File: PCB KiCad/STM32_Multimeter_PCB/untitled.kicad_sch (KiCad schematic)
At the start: 73 parts, among them J6 Barrel_Jack, J7 Conn_01x02_Pin, J8 Barrel_Jack, J9 Barrel_Jack, K1 G6K-2, Q1 CSD19534Q5A, Q10 BC327, Q11 BC327, Q12 BC327, Q13 BC327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

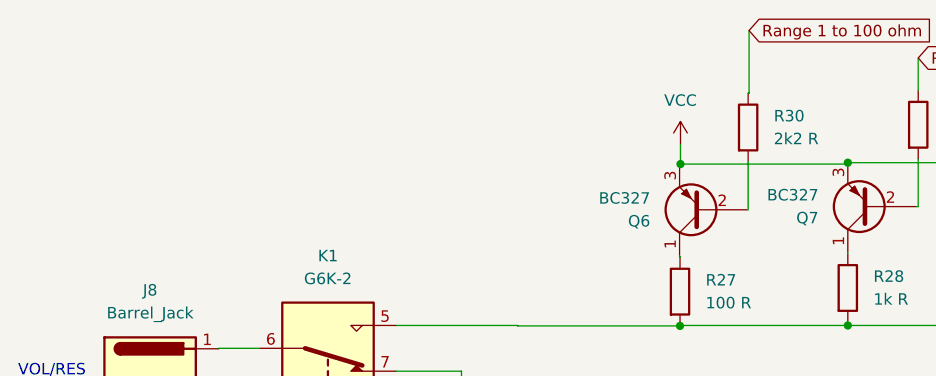
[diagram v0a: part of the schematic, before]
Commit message: Connected measuring circuitry to STM32
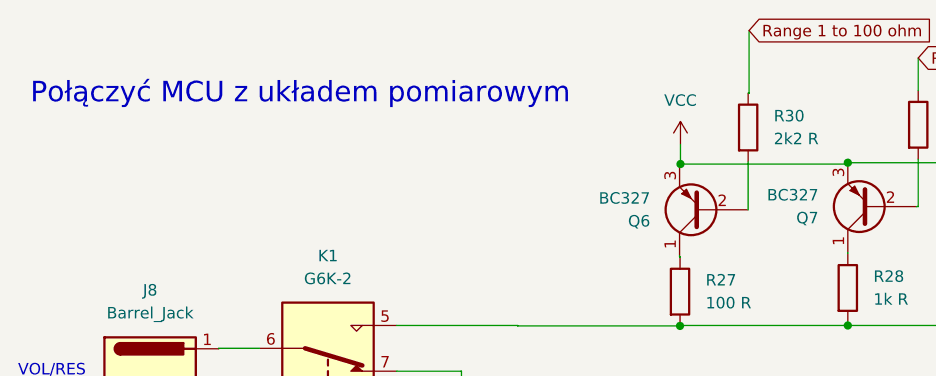
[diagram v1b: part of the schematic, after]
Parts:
- L5: footprint Inductor_SMD:L_Chilisin_BMRB00060650 -> Inductor_SMD:L_Taiyo-Yuden_NR-50xx
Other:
- note added: "Połączyć MCU z układem pomiarowym"
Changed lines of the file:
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@@
     (effects (font (size 1.27 1.27)) (justify left bottom))
+  )
+  (text "Połączyć MCU z układem pomiarowym" (at 14.7828 22.9108 0)
+    (effects (font (size 2.27 2.27)) (justify left bottom))
   )
   (text "COM" (at 186.944 34.4932 0)
@@
       (effects (font (size 1.27 1.27)) (justify left))
     )
-    (property "Footprint" "Inductor_SMD:L_Chilisin_BMRB00060650" (at 221.0308 138.7856 0)
-      (effects (font (size 1.27 1.27)) hide)
-    )
+    (property "Footprint" "Inductor_SMD:L_Taiyo-Yuden_NR-50xx" (at 221.0308 138.7856 0)
+      (effects (font (size 1.27 1.27)) hide)
+    )

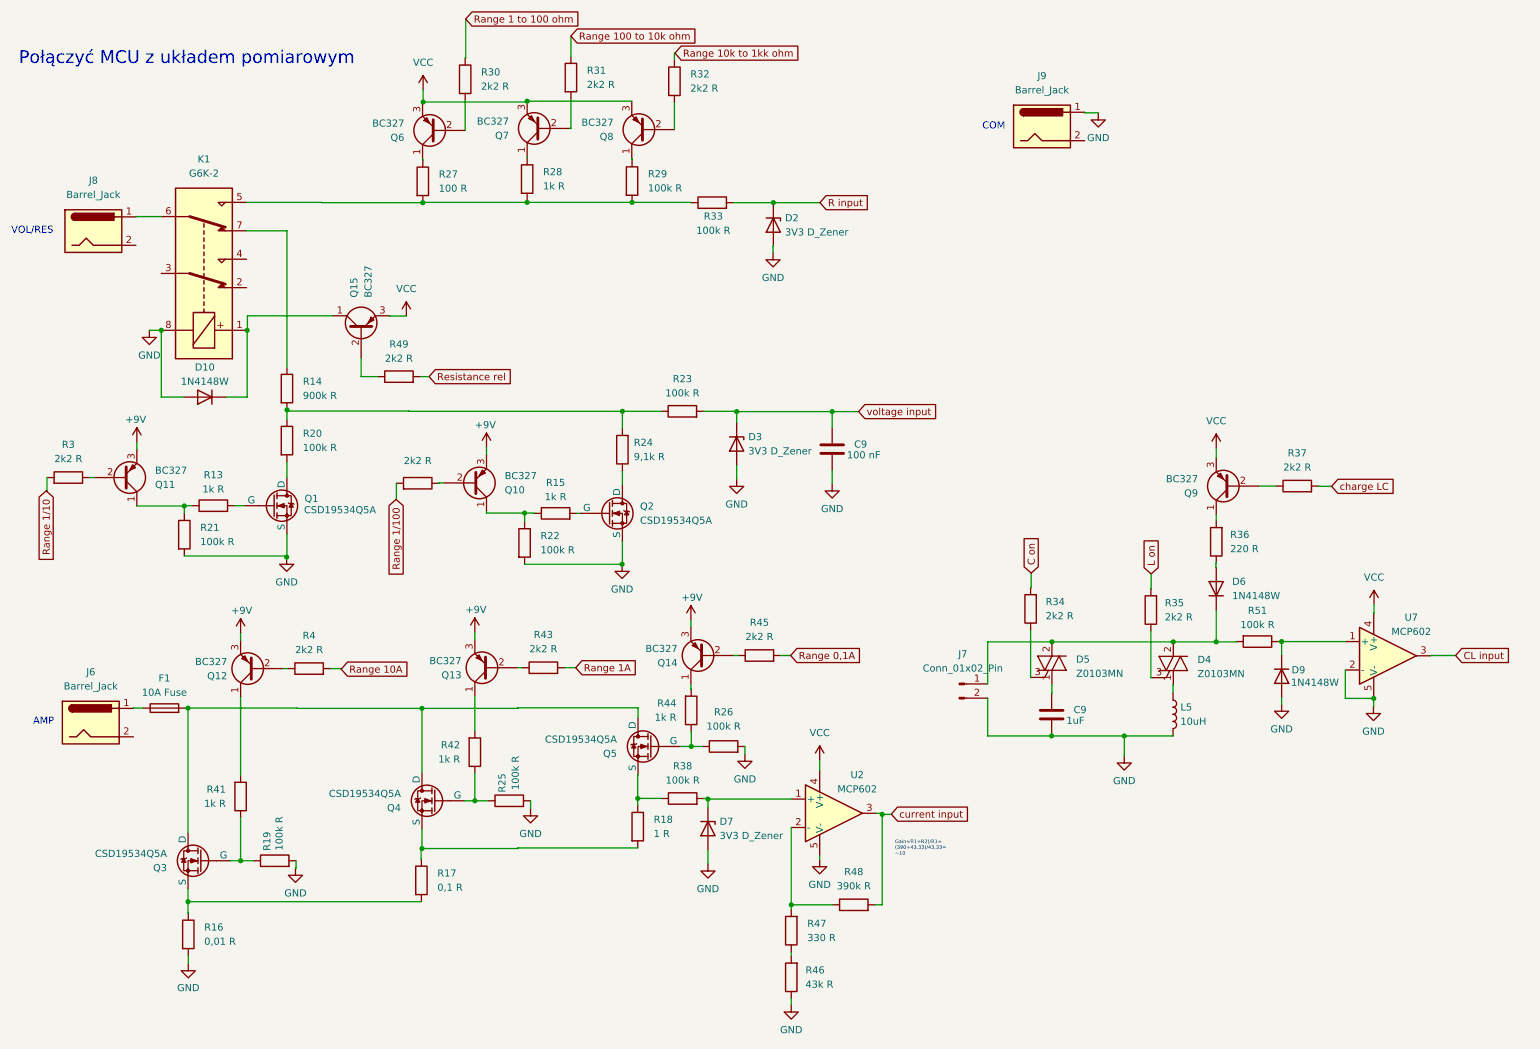
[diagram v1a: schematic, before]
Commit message: Created pcb schematic
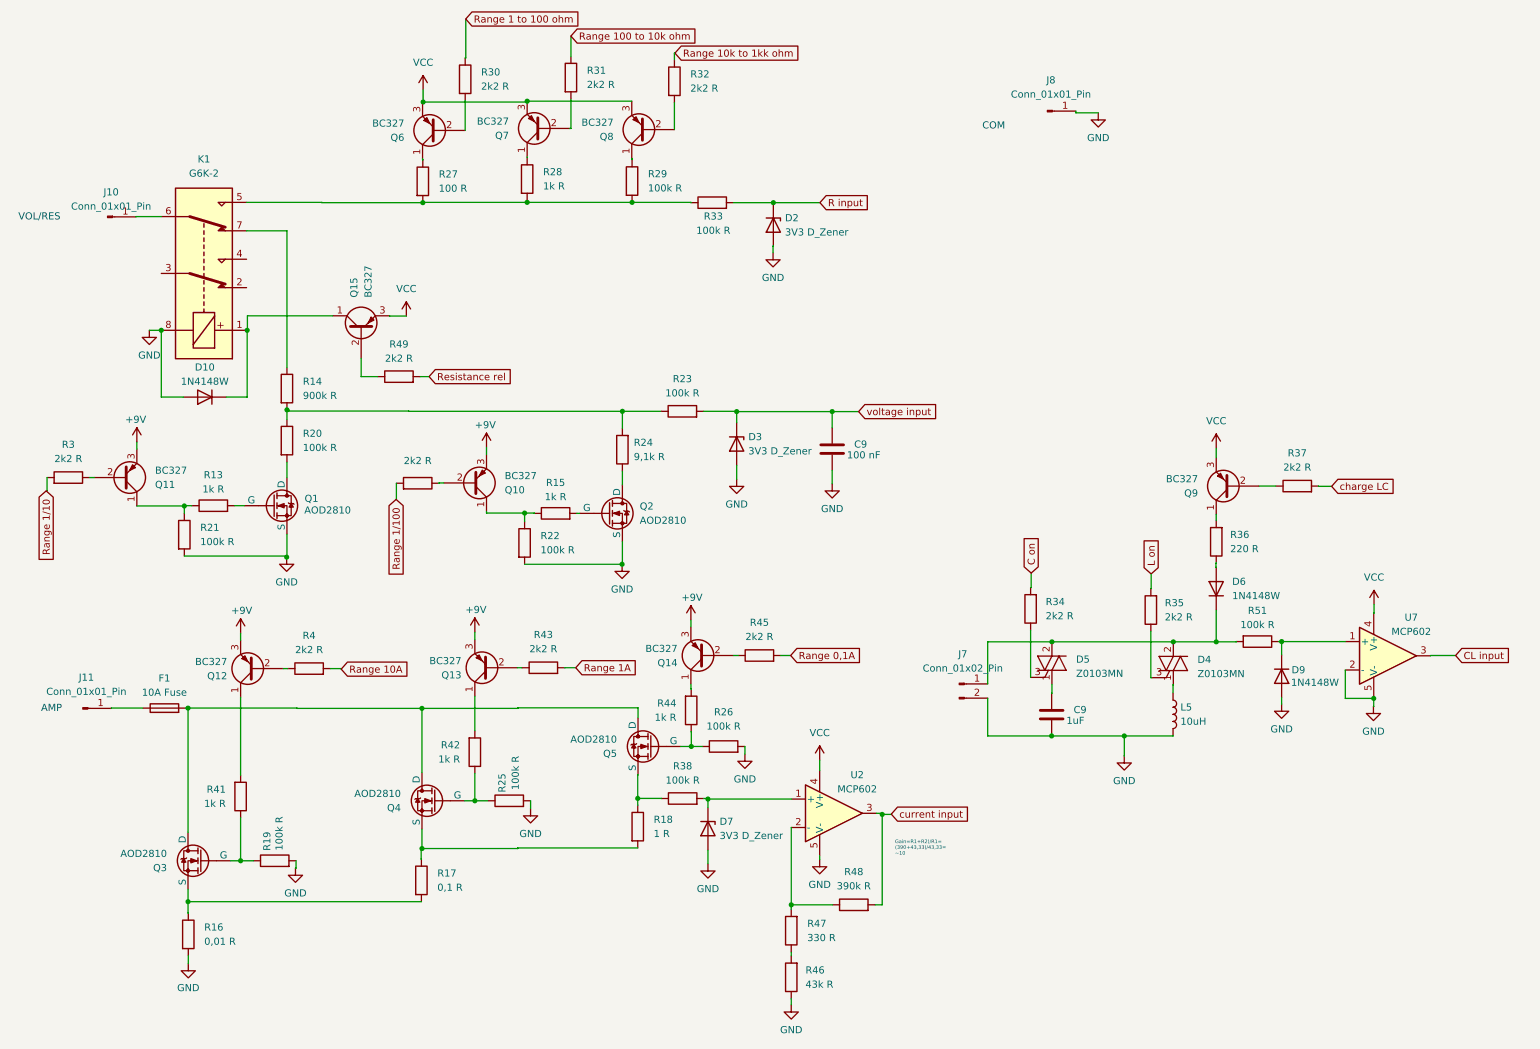
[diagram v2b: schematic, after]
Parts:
- removed J6, J8, J9: Barrel_Jack, Connector_PinHeader_2.54mm:PinHeader_1x01_P2.54mm_Vertical, symbol Connector:Barrel_Jack
- added J10, J11, J8: Conn_01x01_Pin, Connector_PinHeader_2.54mm:PinHeader_1x01_P2.54mm_Vertical, symbol Connector:Conn_01x01_Pin
- Q1, Q2, Q3, Q4, Q5: value CSD19534Q5A -> AOD2810; footprint Package_DFN_QFN:PQFN-8-EP_6x5mm_P1.27mm_Generic -> moje_elementy:TO-252-1
- R16, R17: footprint Resistor_SMD:R_MELF_MMB-0207 -> Resistor_THT:R_Box_L14.0mm_W5.0mm_P9.00mm
- R18: footprint Resistor_SMD:R_MELF_MMB-0207 -> Resistor_THT:R_Axial_DIN0918_L18.0mm_D9.0mm_P25.40mm_Horizontal
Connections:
- net GND: now also J8.1 (Pin_1)
- net at K1.6: now also J10.1 (Pin_1)
- net at F1.1: now also J11.1 (Pin_1)
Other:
- note removed: "Połączyć MCU z układem pomiarowym"

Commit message: routed out signals and power planes
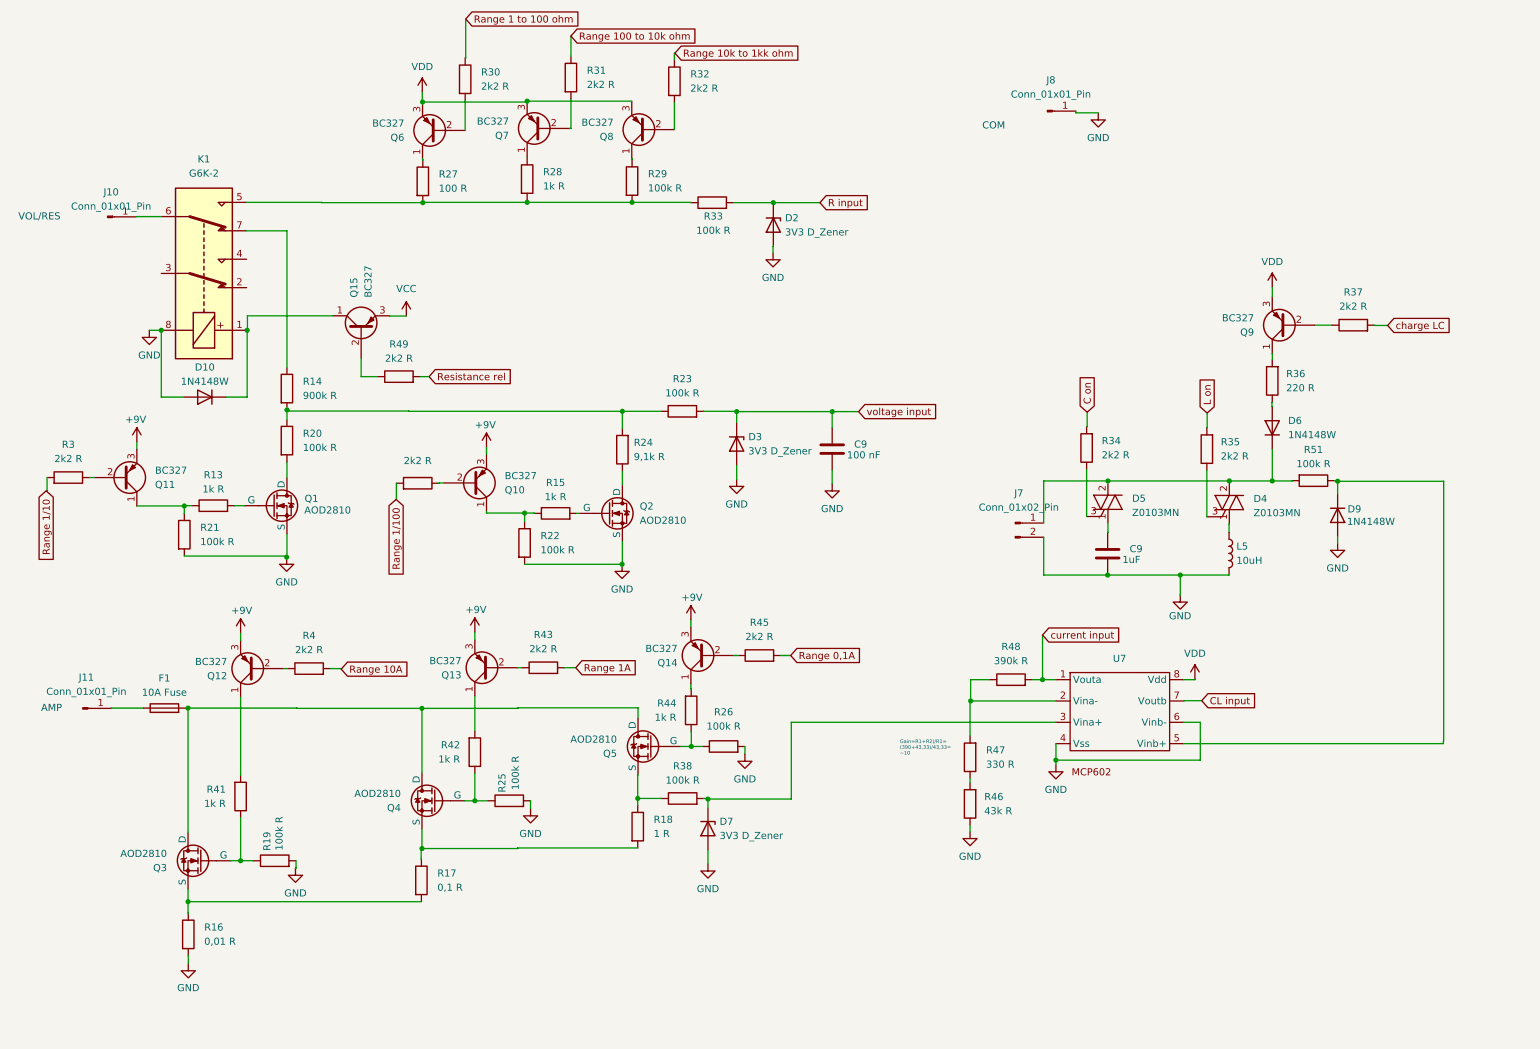
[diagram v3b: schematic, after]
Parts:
- removed U2, U7: MCP602, symbol Simulation_SPICE:OPAMP
- added U7: ~, Package_SO:SOP-8_3.9x4.9mm_P1.27mm, symbol STM32_Bsed_Meter_Library:MCP602
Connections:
- net CL input: now also U7.7 (Voutb)
- net GND: now also U7.4 (Vss), U7.6 (Vinb-)
- net VCC: no longer Q6.3 (E), Q7.3 (E), Q8.3 (E), Q9.3 (E)
- net current input: now also U7.1 (Vouta)
- net at D9.1 (K), R51.1: now also U7.5 (Vinb+)
- net at R47.2, R48.1: now also U7.2 (Vina-)
- net at D7.1 (K), R38.2: now also U7.3 (Vina+)
- new net VDD: Q6.3 (E), Q7.3 (E), Q8.3 (E), Q9.3 (E), U7.8 (Vdd)
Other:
- moved on the sheet: C9, D4, D5, D6, D9, J7, L5, Q9, R34, R35, R36, R37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

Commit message: added missing shop links to the part list
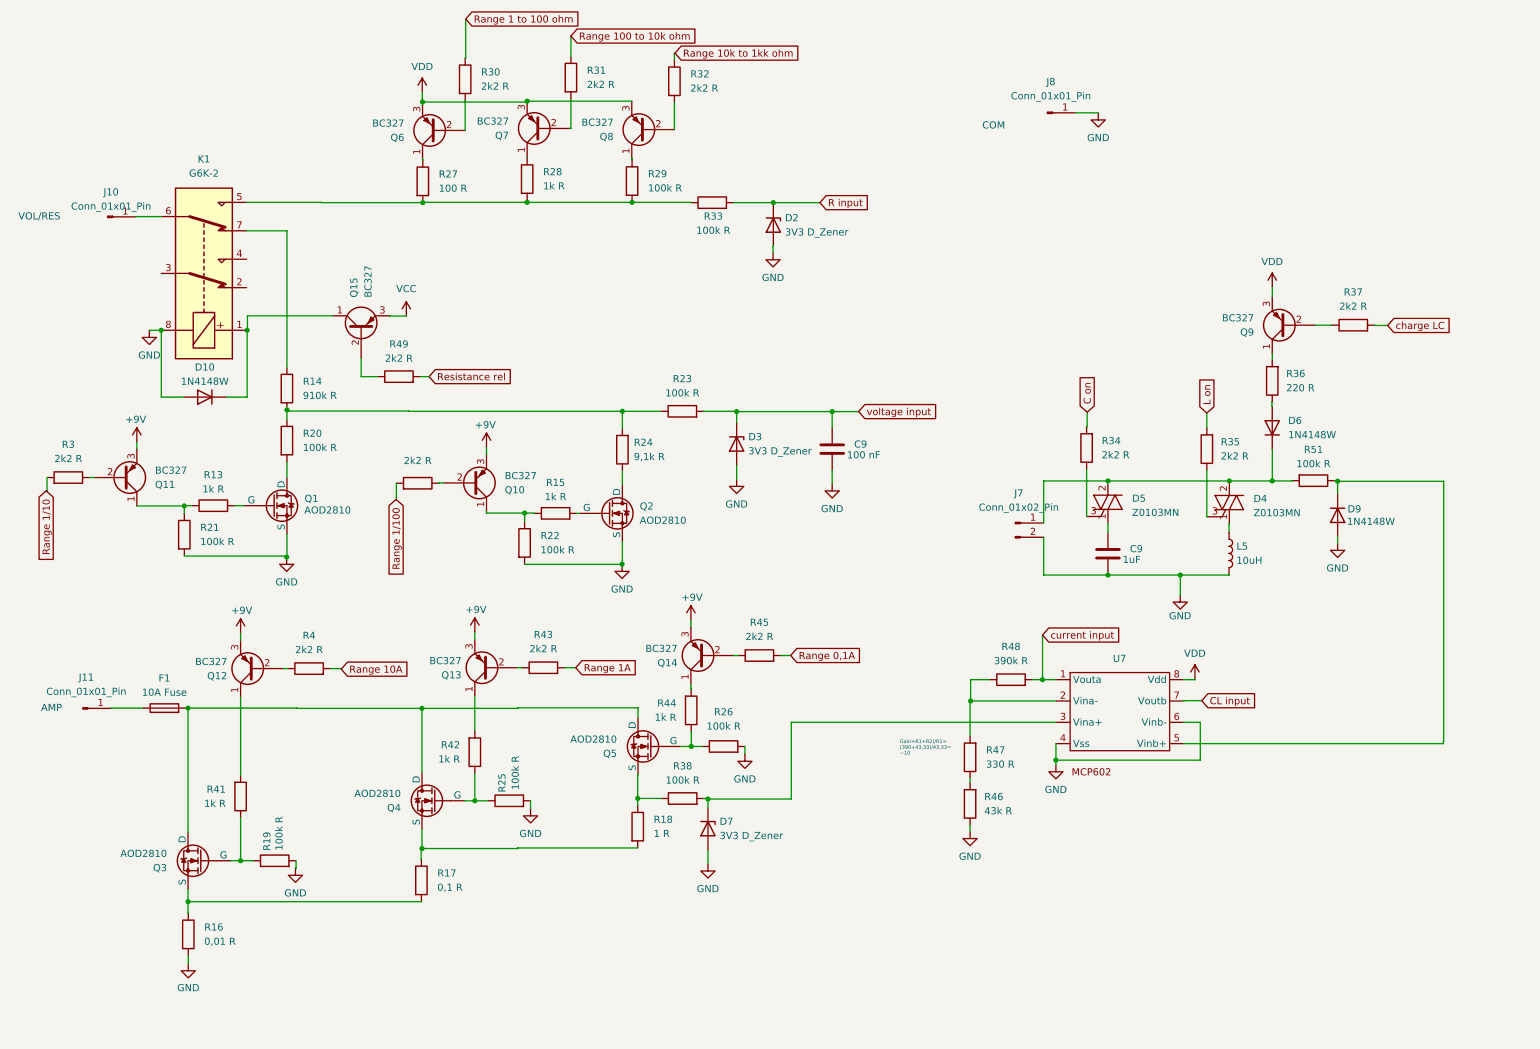
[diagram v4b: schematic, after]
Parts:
- R14: value 900k R -> 910k R
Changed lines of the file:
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@@
   (junction (at 197.7136 132.588) (diameter 0) (color 0 0 0 0)
   )
+  (junction (at 209.3976 113.8936) (diameter 0) (color 0 0 0 0)
+  )
   (junction (at 200.1012 146.9644) (diameter 0) (color 0 0 0 0)
   )
@@
   (junction (at 86.8172 137.7188) (diameter 0) (color 0 0 0 0)
   )
-  (junction (at 209.3468 113.8936) (diameter 0) (color 0 0 0 0)
-  )
   (junction (at 122.5804 111.9632) (diameter 0) (color 0 0 0 0)
   )
@@
     (stroke (width 0) (type default))
   )
-  (wire (pts (xy 209.3468 113.8936) (xy 222.3287 113.8936))
+  (wire (pts (xy 197.9168 113.8936) (xy 209.3976 113.8936))
     (stroke (width 0) (type default))
   )
@@
     (stroke (width 0) (type default))
   )
-  (wire (pts (xy 227.1268 84.9376) (xy 227.1268 87.5792))
+  (wire (pts (xy 227.076 84.9376) (xy 227.076 87.5792))
     (stroke (width 0) (type default))
   )
@@
     (stroke (width 0) (type default))
   )
-  (wire (pts (xy 197.9168 113.8936) (xy 209.3468 113.8936))
-    (stroke (width 0) (type default))
-  )
   (wire (pts (xy 84.4296 84.6328) (xy 84.4296 84.582))
     (stroke (width 0) (type default))
@@
     (stroke (width 0) (type default))
   )
-  (wire (pts (xy 227.1268 87.5792) (xy 227.076 87.5792))
-    (stroke (width 0) (type default))
-  )
   (wire (pts (xy 45.0088 172.2628) (xy 45.0088 174.2948))
     (stroke (width 0) (type default))
@@
     (stroke (width 0) (type default))
   )
-  (wire (pts (xy 209.3976 106.2736) (xy 209.3468 106.2736))
-    (stroke (width 0) (type default))
-  )
   (wire (pts (xy 122.6312 95.3008) (xy 122.6312 97.79))
     (stroke (width 0) (type default))
@@
     (stroke (width 0) (type default))
   )
-  (wire (pts (xy 203.6572 31.2928) (xy 203.6572 30.988))
-    (stroke (width 0) (type default))
-  )
   (wire (pts (xy 131.9276 20.6248) (xy 132.0292 20.6248))
     (stroke (width 0) (type default))
@@
   )
   (wire (pts (xy 113.4364 28.8036) (xy 113.4364 34.0868))
+    (stroke (width 0) (type default))
+  )
+  (wire (pts (xy 209.3976 113.8936) (xy 222.3287 113.8936))
     (stroke (width 0) (type default))
   )
@@
     )
   )
-  (global_label "L on" (shape input) (at 227.1268 84.9376 90) (fields_autoplaced)
+  (global_label "L on" (shape input) (at 227.076 84.9376 90) (fields_autoplaced)
     (effects (font (size 1.27 1.27)) (justify left))
-    (property "Intersheetrefs" "${INTERSHEET_REFS}" (at 227.1268 77.6587 90)
+    (property "Intersheetrefs" "${INTERSHEET_REFS}" (at 227.076 77.6587 90)
       (effects (font (size 1.27 1.27)) (justify left) hide)
     )
@@
       (effects (font (size 1.27 1.27)) (justify left))
     )
-    (property "Value" "900k R" (at 65.532 81.8388 0)
+    (property "Value" "910k R" (at 65.532 81.8388 0)
       (effects (font (size 1.27 1.27)) (justify left))
     )
@@
     )
   )
-  (symbol (lib_id "Device:C") (at 209.3468 110.0836 0) (unit 1)
+  (symbol (lib_id "Device:C") (at 209.3976 110.0836 0) (unit 1)
     (in_bom yes) (on_board yes) (dnp no)
-    (property "Reference" "C9" (at 215.5952 109.22 0)
+    (property "Reference" "C9" (at 215.646 109.22 0)
       (effects (font (size 1.27 1.27)) (justify right))
     )
-    (property "Value" "1uF" (at 211.9884 111.1504 0)
-      (effects (font (size 1.27 1.27)) (justify left))
-    )
-    (property "Footprint" "Capacitor_SMD:C_0805_2012Metric" (at 210.312 113.8936 0)
-      (effects (font (size 1.27 1.27)) hide)
-    )
-    (property "Datasheet" "~" (at 209.3468 110.0836 0)
+    (property "Value" "1uF" (at 212.0392 111.1504 0)
+      (effects (font (size 1.27 1.27)) (justify left))
+    )
+    (property "Footprint" "Capacitor_SMD:C_0805_2012Metric" (at 210.3628 113.8936 0)
+      (effects (font (size 1.27 1.27)) hide)
+    )
+    (property "Datasheet" "~" (at 209.3976 110.0836 0)
       (effects (font (size 1.27 1.27)) hide)
     )
@@
     )
   )
-  (symbol (lib_id "Connector:Conn_01x01_Pin") (at 198.5772 30.988 0) (unit 1)
-    (in_bom yes) (on_board yes) (dnp no) (fields_autoplaced)
-    (property "Reference" "J8" (at 199.2122 25.4508 0)
-      (effects (font (size 1.27 1.27)))
-    )
-    (property "Value" "Conn_01x01_Pin" (at 199.2122 27.9908 0)
-      (effects (font (size 1.27 1.27)))
-    )
-    (property "Footprint" "Connector_PinHeader_2.54mm:PinHeader_1x01_P2.54mm_Vertical" (at 198.5772 30.988 0)
-      (effects (font (size 1.27 1.27)) hide)
-    )
-    (property "Datasheet" "~" (at 198.5772 30.988 0)
-      (effects (font (size 1.27 1.27)) hide)
-    )
+  (symbol (lib_id "Connector:Conn_01x01_Pin") (at 198.5772 31.2928 0) (unit 1)
+    (in_bom yes) (on_board yes) (dnp no) (fields_autoplaced)
+    (property "Reference" "J8" (at 199.2122 25.7556 0)
+      (effects (font (size 1.27 1.27)))
+    )
+    (property "Value" "Conn_01x01_Pin" (at 199.2122 28.2956 0)
+      (effects (font (size 1.27 1.27)))
+    )
+    (property "Footprint" "Connector_PinHeader_2.54mm:PinHeader_1x01_P2.54mm_Vertical" (at 198.5772 31.2928 0)
+      (effects (font (size 1.27 1.27)) hide)
+    )
+    (property "Datasheet" "~" (at 198.5772 31.2928 0)
+      (effects (font (size 1.27 1.27)) hide)
+    )
